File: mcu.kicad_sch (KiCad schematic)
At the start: 19 parts, among them J1 GSB1C211110DS1HR, J2 Conn_01x04_Pin, J3 Conn_01x04_Pin, SW1 SW_SPDT, U1 TPS7B8133DRVR, U2 STM32L053C8T6

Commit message: adjust paths for kicanvas
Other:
- company: (none) -> https://github.com/Challmymind
- title: (none) -> Keyboard based on STM32L0xx
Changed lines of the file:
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@@
 	(generator_version "8.0")
 	(paper "A4")
+	(title_block
+		(title "Keyboard based on STM32L0xx")
+		(date "2024-04-28")
+		(rev "0.1")
+		(company "https://github.com/Challmymind")
+	)
 	(junction
 		(at 162.56 64.77)

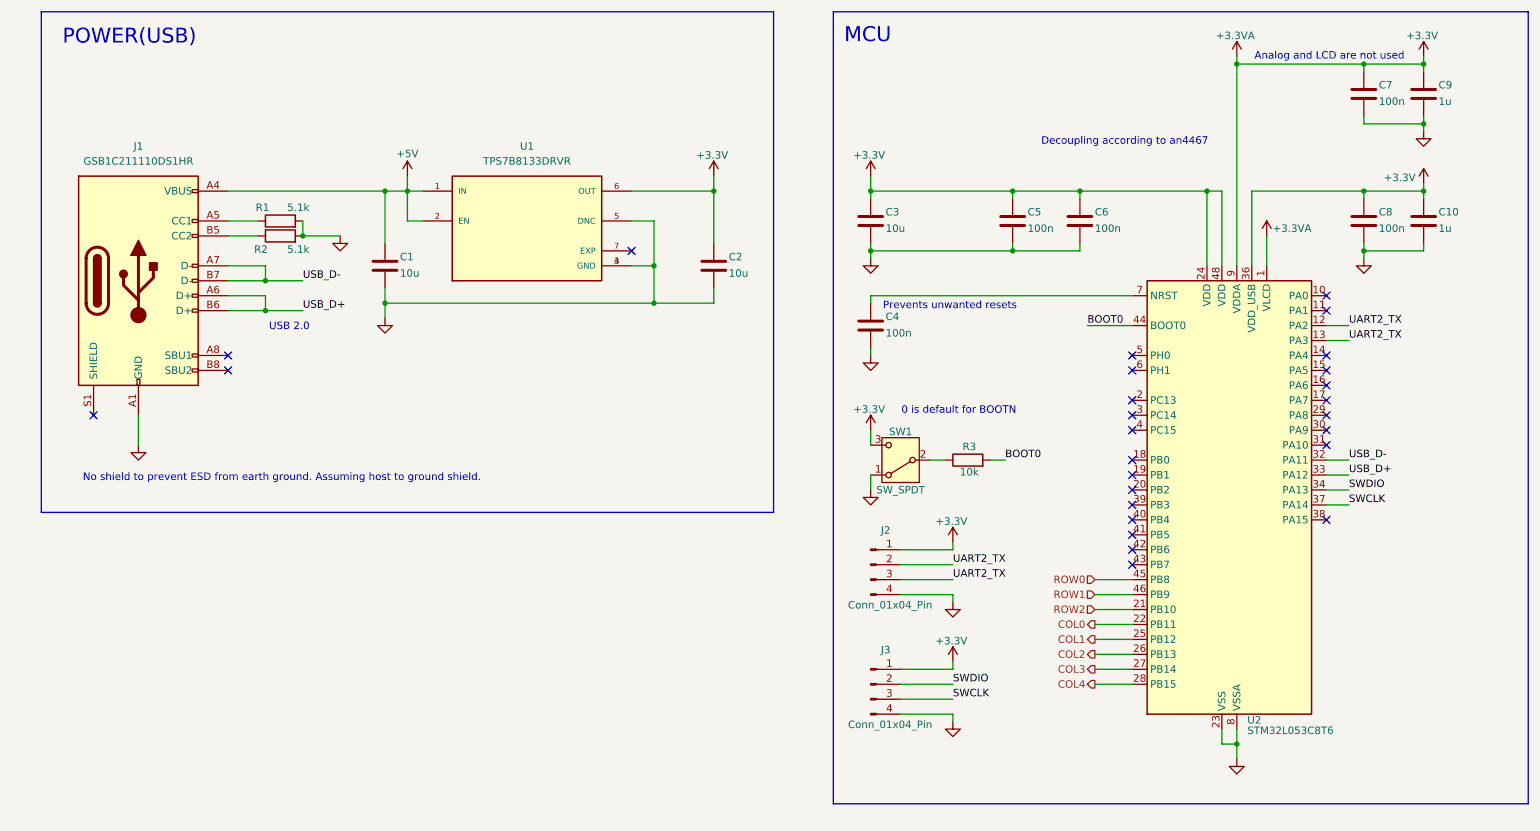
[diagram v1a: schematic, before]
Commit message: moved usb to another sheet, cleared ERC violations
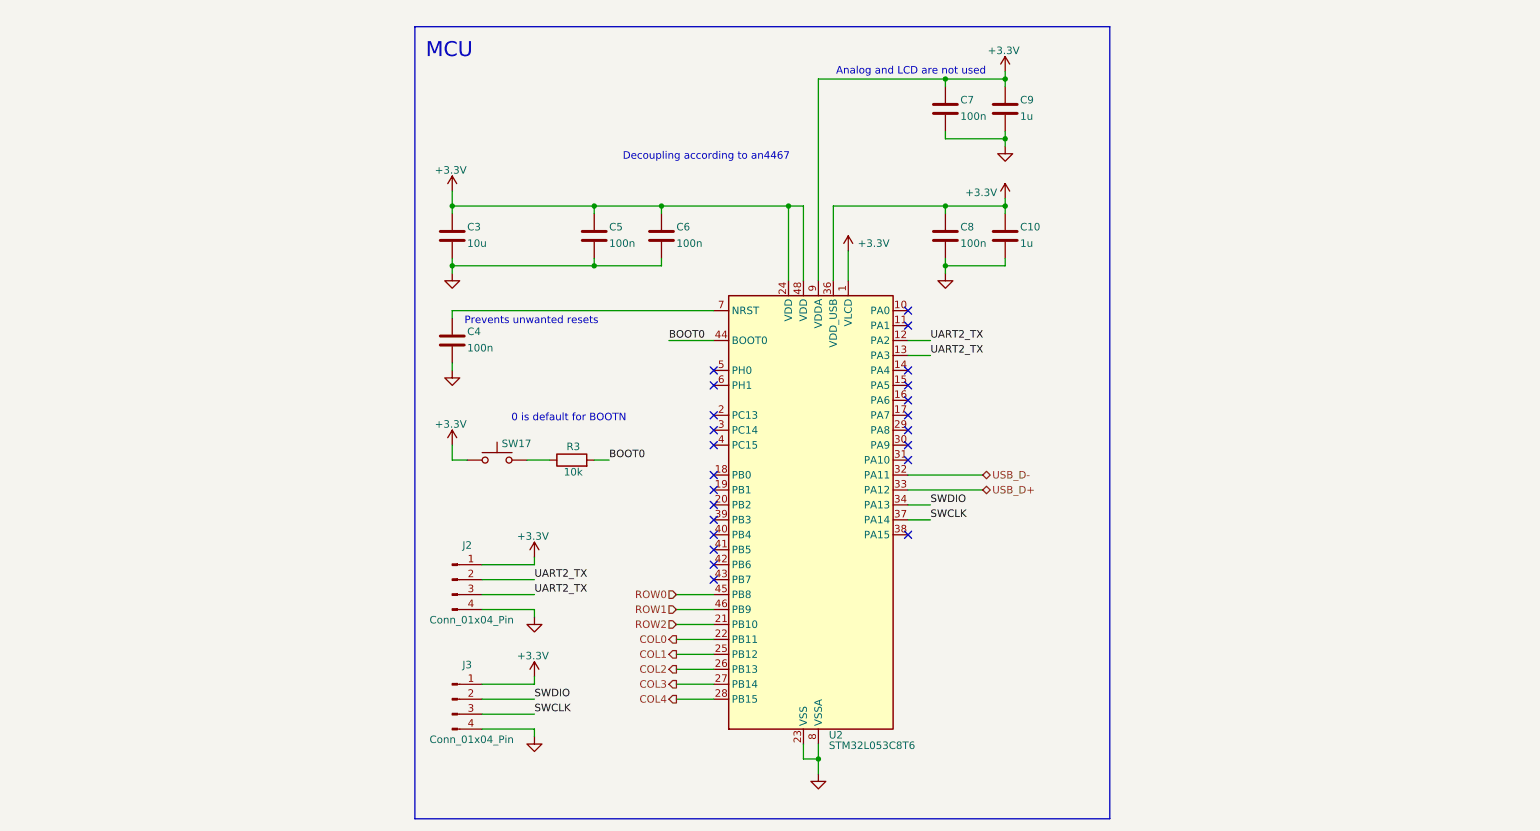
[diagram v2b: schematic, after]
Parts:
- removed C1, C2: 10u, symbol Device:C
- removed J1: GSB1C211110DS1HR, symbol Connector:USB_C_Receptacle_USB2.0_16P
- removed R1, R2: 5.1k, symbol Device:R
- removed SW1: SW_SPDT, symbol Switch:SW_SPDT
- removed U1: TPS7B8133DRVR, TPS7B8133DRVR:SON65P200X200X80-7N, symbol TPS7B8133DRVR:TPS7B8133DRVR
- added SW17: SW_Push, symbol Switch:SW_Push
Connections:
- net +3.3V: now also SW17.1
- net at R3.1: now also SW17.2
- no-connect marks 27 -> 23
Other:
- note removed: "No shield to prevent ESD from earth ground. Assuming host to ground shield."
- note removed: "POWER(USB)"
- note removed: "USB 2.0"
- moved on the sheet: C10, C3, C4, C5, C6, C7, C8, C9, J2, J3, R3, U2

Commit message: completed 0.1 schematic design
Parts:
- added C10: 100n, Capacitor_SMD:C_0402_1005Metric, symbol Device:C
- added C11: 1u, Capacitor_SMD:C_0402_1005Metric, symbol Device:C
- C12: renamed from C4; footprint (none) -> Capacitor_SMD:C_0402_1005Metric
- C3: renamed from C5; footprint (none) -> Capacitor_SMD:C_0402_1005Metric
- C4: renamed from C6; footprint (none) -> Capacitor_SMD:C_0402_1005Metric
- C5: renamed from C3; footprint (none) -> Capacitor_SMD:C_0603_1608Metric
- C6: renamed from C7; footprint (none) -> Capacitor_SMD:C_0402_1005Metric
- C7: renamed from C9; footprint (none) -> Capacitor_SMD:C_0402_1005Metric
- C8: footprint (none) -> Capacitor_SMD:C_0402_1005Metric
- C9: renamed from C10; footprint (none) -> Capacitor_SMD:C_0402_1005Metric
- J2, J3: footprint (none) -> Connector_PinHeader_2.54mm:PinHeader_1x04_P2.54mm_Vertical
- R3: footprint (none) -> Resistor_SMD:R_0402_1005Metric
- SW16: renamed from SW17; footprint (none) -> Diode_SMD:D_0805_2012Metric
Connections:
- net +3.3V: now also C10.1, C11.1
- net GND: now also C10.2, C11.2; no longer C8.2
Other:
- note added: "Additional decoupling capacitators for VLCD"
- note added: "Prevents DRC from throwing errors"

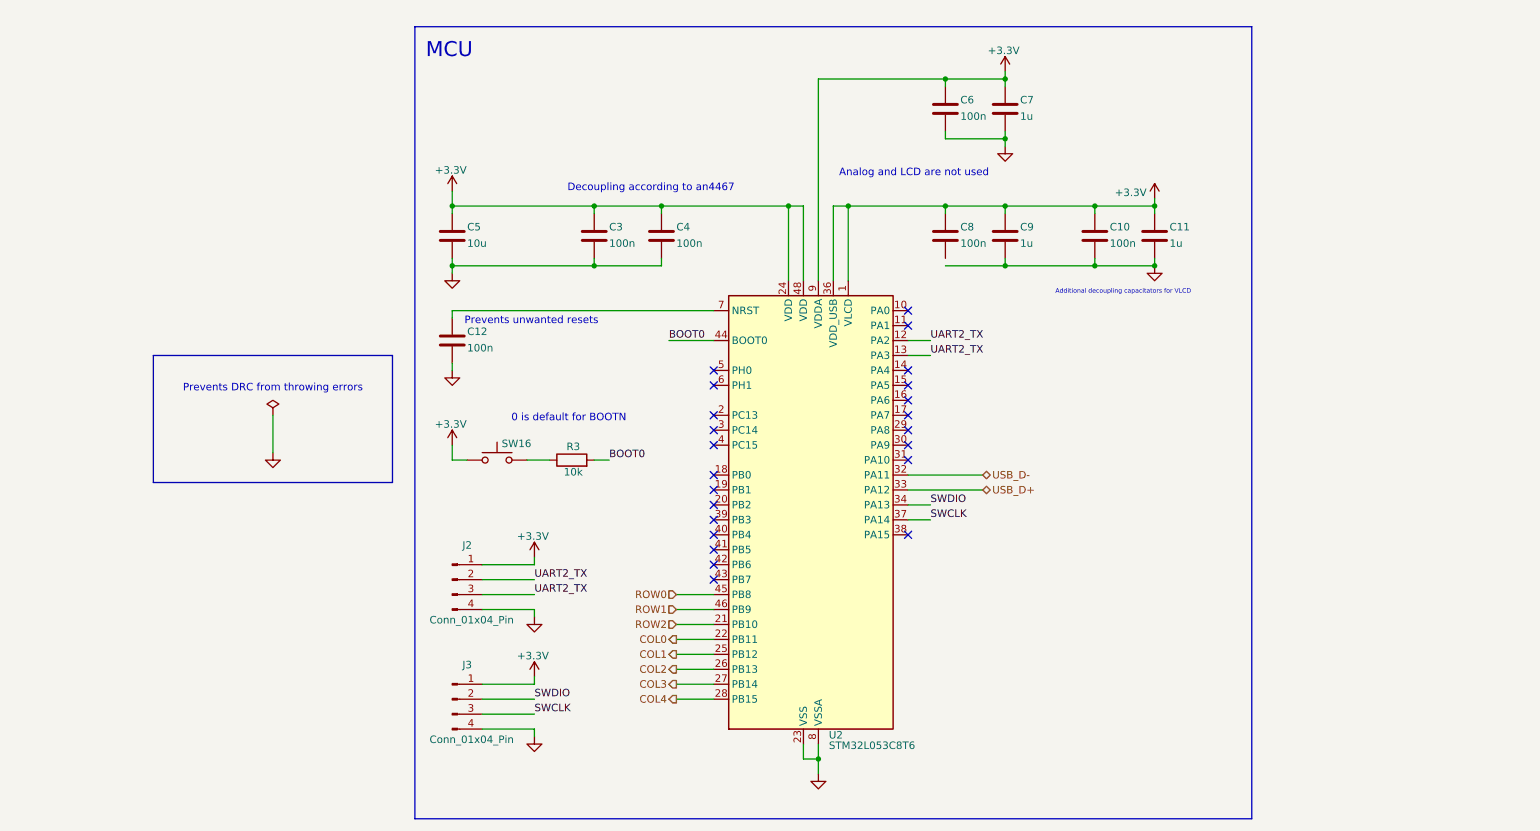
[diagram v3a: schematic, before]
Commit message: switched to bigger matrix, adjusted mcu pins, started pcb layout
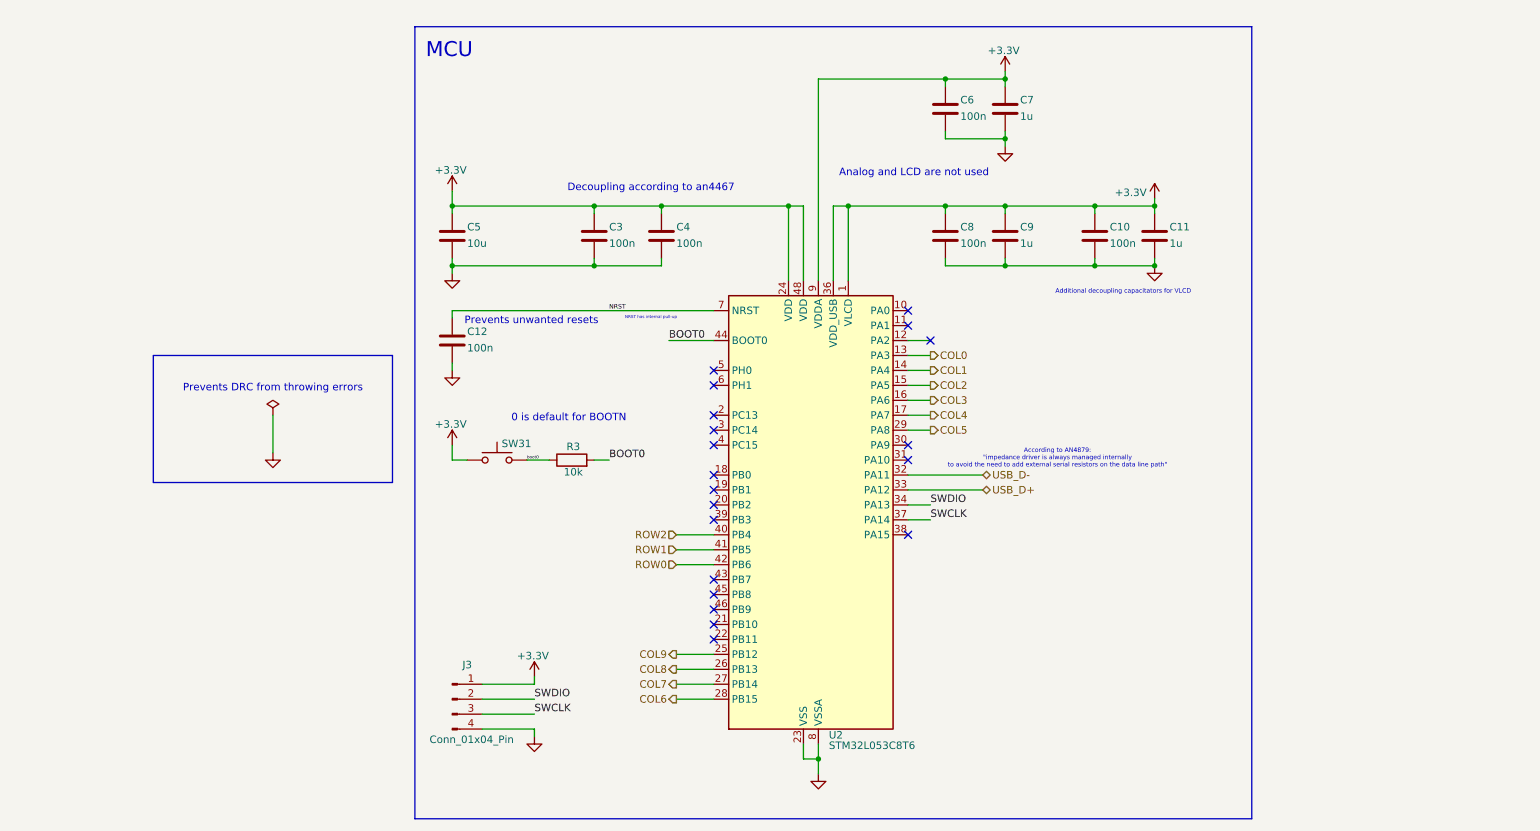
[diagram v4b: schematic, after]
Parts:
- removed J2: Conn_01x04_Pin, Connector_PinHeader_2.54mm:PinHeader_1x04_P2.54mm_Vertical, symbol Connector:Conn_01x04_Pin
- renumbered SW16 to SW31
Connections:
- net COL0: now also U2.13 (PA3); no longer U2.22 (PB11)
- net COL1: now also U2.14 (PA4); no longer U2.25 (PB12)
- net COL2: now also U2.15 (PA5); no longer U2.26 (PB13)
- net COL3: now also U2.16 (PA6); no longer U2.27 (PB14)
- net COL4: now also U2.17 (PA7); no longer U2.28 (PB15)
- net GND: now also C8.2
- net ROW0: now also U2.42 (PB6); no longer U2.45 (PB8)
- net ROW1: now also U2.41 (PB5); no longer U2.46 (PB9)
- net ROW2: now also U2.40 (PB4); no longer U2.21 (PB10)
- net boot0: now reaches R3.1, SW31.2
- net NRST: now reaches C12.1, U2.7 (NRST)
- net COL5: now reaches U2.29 (PA8)
- net UART2_TX: no longer names the net of U2.12 (PA2)
- net UART2_TX: no longer U2.13 (PA3)
- new net COL6: U2.28 (PB15)
- new net COL7: U2.27 (PB14)
- new net COL8: U2.26 (PB13)
- new net COL9: U2.25 (PB12)
- no-connect marks 23 -> 20
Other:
- note added: "According to AN4879: "impedance driver is always managed internally to avoid the need to add external serial resistors on the data line path""
- note added: "NRST has internal pull-up"

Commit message: added routing
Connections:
- net COL5: now also U2.25 (PB12); no longer U2.29 (PA8)
- net COL6: now also U2.26 (PB13); no longer U2.28 (PB15)
- net COL8: now also U2.28 (PB15); no longer U2.26 (PB13)
- net COL9: now also U2.29 (PA8); no longer U2.25 (PB12)
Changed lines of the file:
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@@
 	(hierarchical_label "COL6"
 		(shape output)
-		(at 129.54 140.97 180)
+		(at 129.54 135.89 180)
 		(fields_autoplaced yes)
 		(effects
@@
 	(hierarchical_label "COL5"
 		(shape output)
-		(at 172.72 95.25 0)
+		(at 129.54 133.35 180)
 		(fields_autoplaced yes)
 		(effects
@@
 				(size 1.27 1.27)
 			)
-			(justify left)
+			(justify right)
 		)
 	)
 	(hierarchical_label "COL8"
 		(shape output)
-		(at 129.54 135.89 180)
+		(at 129.54 140.97 180)
 		(fields_autoplaced yes)
 		(effects
@@
 	(hierarchical_label "COL9"
 		(shape output)
-		(at 129.54 133.35 180)
+		(at 172.72 95.25 0)
 		(fields_autoplaced yes)
 		(effects
@@
 				(size 1.27 1.27)
 			)
-			(justify right)
+			(justify left)
 		)
 	)

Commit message: re-done whole pcb
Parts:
- removed C10: 100n, Capacitor_SMD:C_0402_1005Metric, symbol Device:C
- removed C11: 1u, Capacitor_SMD:C_0402_1005Metric, symbol Device:C
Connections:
- net COL0: now also U2.2 (PC13); no longer U2.13 (PA3)
- net COL1: now also U2.42 (PB6); no longer U2.14 (PA4)
- net COL2: now also U2.41 (PB5); no longer U2.15 (PA5)
- net COL3: now also U2.4 (PC15); no longer U2.16 (PA6)
- net COL4: now also U2.3 (PC14); no longer U2.17 (PA7)
- net COL5: now also U2.26 (PB13); no longer U2.25 (PB12)
- net COL6: now also U2.25 (PB12); no longer U2.26 (PB13)
- net ROW0: now also U2.16 (PA6); no longer U2.42 (PB6)
- net ROW1: now also U2.17 (PA7); no longer U2.41 (PB5)
- net ROW2: now also U2.38 (PA15); no longer U2.40 (PB4)
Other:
- note removed: "Additional decoupling capacitators for VLCD"
